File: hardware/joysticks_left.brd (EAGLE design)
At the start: 64.8 x 87.6 mm, 10 parts, among them IC1 MEGA16-M

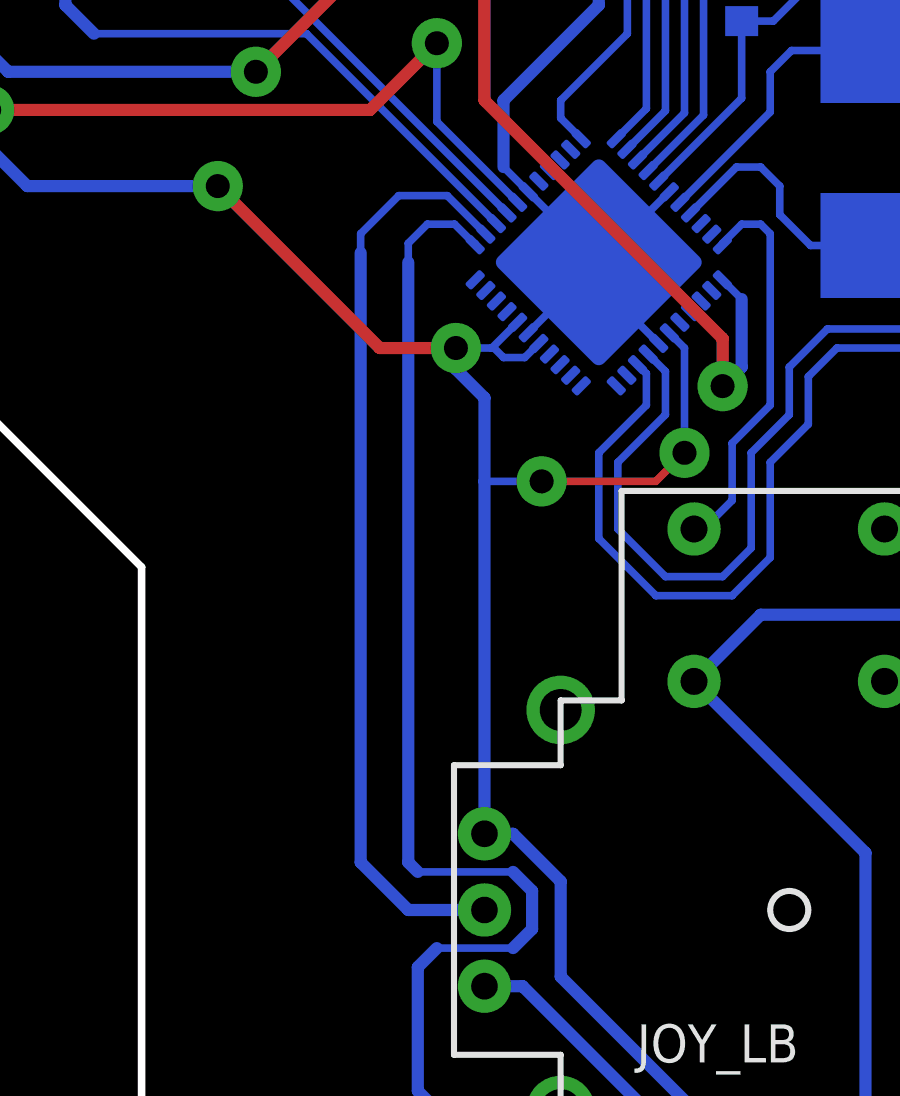
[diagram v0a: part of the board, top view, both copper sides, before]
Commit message: added mode selection jumper (SPI/I2C)
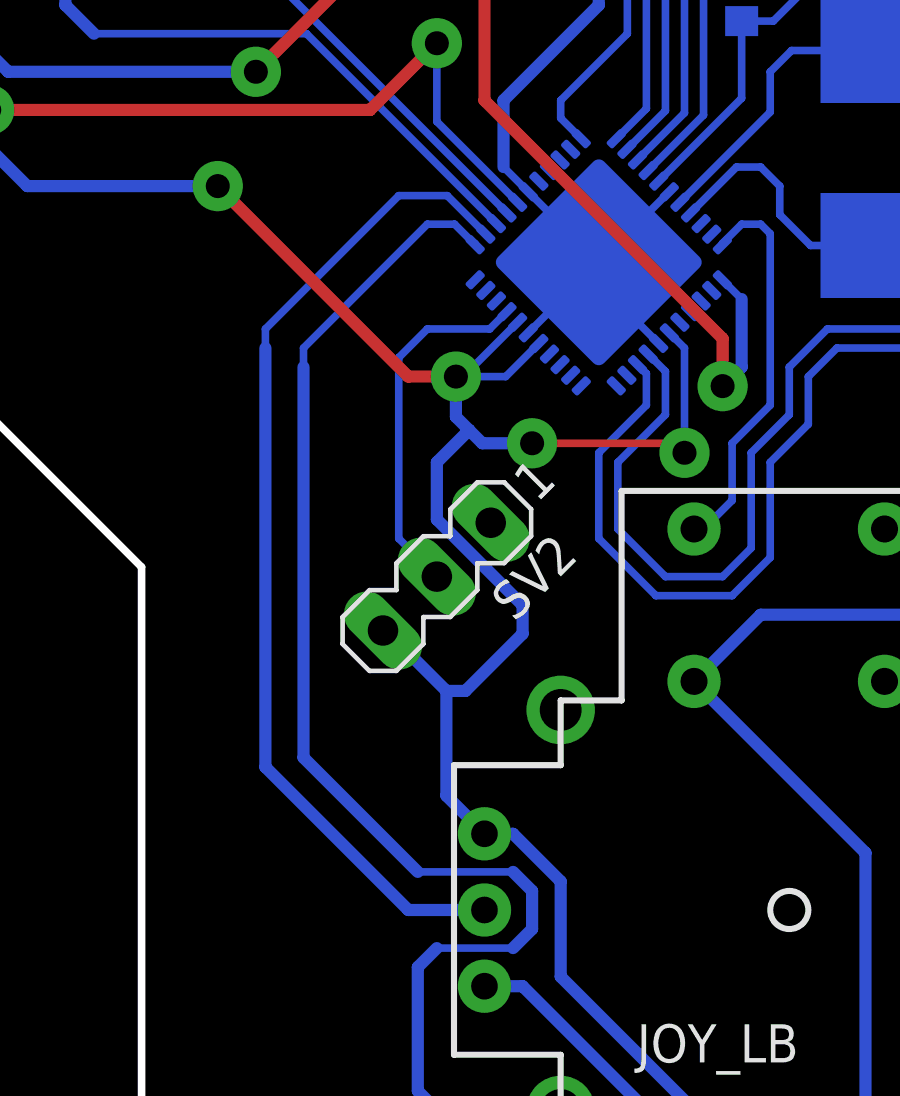
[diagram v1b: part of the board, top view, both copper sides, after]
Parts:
- added SV2: (no value), con-lstb:MA03-1
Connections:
- new net MD_SEL: IC1.30, SV2.2
- net GND: now also SV2.1
- net VCC: now also SV2.3
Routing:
- net MD_SEL: track 0.00 -> 12.1 mm
- net VCC: track 210.4 -> 218.4 mm
- net JOY_LB_H: track 54.8 -> 57.7 mm
- net JOY_LB_V: track 31.0 -> 33.6 mm
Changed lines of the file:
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@@
 <element name="U$2" library="holes" package="3,0" value="" x="30.1625" y="77.47"/>
 <element name="U$3" library="holes" package="3,0" value="" x="40.64" y="2.54"/>
+<element name="SV2" library="con-lstb" package="MA03-1" value="" x="28.8925" y="31.4325" rot="R225">
+<attribute name="OC_NEWARK" value="unknown" x="28.8925" y="31.4325" size="1.778" layer="27" rot="R225" display="off"/>
+<attribute name="MPN" value="" x="28.8925" y="31.4325" size="1.778" layer="27" rot="R225" display="off"/>
+<attribute name="MF" value="" x="28.8925" y="31.4325" size="1.778" layer="27" rot="R225" display="off"/>
+<attribute name="OC_FARNELL" value="unknown" x="28.8925" y="31.4325" size="1.778" layer="27" rot="R225" display="off"/>
+</element>
 </elements>
 <signals>
@@
 <vertex x="10.16" y="83.82"/>
 </polygon>
+<contactref element="SV2" pad="1"/>
 </signal>
 <signal name="VCC">
@@
 <wire x1="33.02" y1="18.0975" x2="38.1" y2="13.0175" width="0.4064" layer="16"/>
 <wire x1="38.1" y1="13.0175" x2="38.1" y2="10.16" width="0.4064" layer="16"/>
-<wire x1="30.48" y1="37.392890625" x2="30.48" y2="34.6075" width="0.4064" layer="16"/>
-<wire x1="30.48" y1="34.6075" x2="30.48" y2="22.86" width="0.4064" layer="16"/>
 <wire x1="31.58531875" y1="43.907575" x2="28.8925" y2="46.60039375" width="0.254" layer="16"/>
 <wire x1="28.8925" y1="46.60039375" x2="28.8925" y2="49.2125" width="0.254" layer="16"/>
@@
 <wire x1="22.86" y1="48.26" x2="14.605" y2="48.26" width="0.4064" layer="16"/>
 <wire x1="14.605" y1="48.26" x2="13.97" y2="48.895" width="0.4064" layer="16"/>
-<via x="29.5275" y="39.0525" extent="1-16" drill="0.8" diameter="1.6764"/>
-<wire x1="29.5275" y1="39.0525" x2="26.9875" y2="39.0525" width="0.4064" layer="1"/>
-<wire x1="26.9875" y1="39.0525" x2="21.59" y2="44.45" width="0.4064" layer="1"/>
+<via x="29.5275" y="38.1" extent="1-16" drill="0.8" diameter="1.6764"/>
+<wire x1="29.5275" y1="38.1" x2="27.94" y2="38.1" width="0.4064" layer="1"/>
+<wire x1="27.94" y1="38.1" x2="21.59" y2="44.45" width="0.4064" layer="1"/>
 <via x="21.59" y="44.45" extent="1-16" drill="0.8" diameter="1.6764"/>
 <wire x1="21.59" y1="44.45" x2="15.24" y2="44.45" width="0.4064" layer="16"/>
 <wire x1="15.24" y1="44.45" x2="13.97" y2="45.72" width="0.4064" layer="16"/>
 <wire x1="13.97" y1="45.72" x2="13.97" y2="46.99" width="0.4064" layer="16"/>
-<wire x1="30.48" y1="37.392890625" x2="29.5275" y2="38.345390625" width="0.4064" layer="16"/>
-<wire x1="29.5275" y1="38.345390625" x2="29.5275" y2="39.0525" width="0.4064" layer="16"/>
-<wire x1="31.58531875" y1="39.912421875" x2="30.725396875" y2="39.0525" width="0.254" layer="16"/>
-<wire x1="30.725396875" y1="39.0525" x2="29.5275" y2="39.0525" width="0.254" layer="16"/>
-<wire x1="32.292425" y1="39.205315625" x2="31.822109375" y2="38.735" width="0.254" layer="16"/>
-<wire x1="31.822109375" y1="38.735" x2="31.115" y2="38.735" width="0.254" layer="16"/>
-<wire x1="31.115" y1="38.735" x2="30.7975" y2="39.0525" width="0.254" layer="16"/>
-<wire x1="30.7975" y1="39.0525" x2="30.725396875" y2="39.0525" width="0.254" layer="16"/>
+<wire x1="29.5275" y1="36.757890625" x2="29.5275" y2="38.1" width="0.4064" layer="16"/>
 <wire x1="36.64113125" y1="39.55886875" x2="37.1475" y2="39.0525" width="0.254" layer="16"/>
 <wire x1="37.1475" y1="39.0525" x2="37.1475" y2="35.56" width="0.254" layer="16"/>
 <via x="37.1475" y="35.56" extent="1-16" drill="0.8" diameter="1.6764"/>
-<wire x1="37.1475" y1="35.56" x2="36.195" y2="34.6075" width="0.254" layer="1"/>
-<wire x1="36.195" y1="34.6075" x2="32.385" y2="34.6075" width="0.254" layer="1"/>
-<via x="32.385" y="34.6075" extent="1-16" drill="0.8" diameter="1.6764"/>
-<wire x1="32.385" y1="34.6075" x2="30.48" y2="34.6075" width="0.254" layer="16"/>
+<wire x1="37.1475" y1="35.56" x2="36.83" y2="35.8775" width="0.254" layer="1"/>
+<wire x1="36.83" y1="35.8775" x2="32.0675" y2="35.8775" width="0.254" layer="1"/>
+<via x="32.0675" y="35.8775" extent="1-16" drill="0.8" diameter="1.6764"/>
 <wire x1="51.1175" y1="45.72" x2="53.34" y2="45.72" width="0.254" layer="16"/>
+<contactref element="SV2" pad="3"/>
+<wire x1="31.58531875" y1="39.912421875" x2="29.772896875" y2="38.1" width="0.254" layer="16"/>
+<wire x1="29.772896875" y1="38.1" x2="29.5275" y2="38.1" width="0.254" layer="16"/>
+<wire x1="32.292425" y1="39.205315625" x2="31.187109375" y2="38.1" width="0.254" layer="16"/>
+<wire x1="31.187109375" y1="38.1" x2="29.5275" y2="38.1" width="0.254" layer="16"/>
+<wire x1="29.5275" y1="36.757890625" x2="29.967696875" y2="36.31769375" width="0.4064" layer="16"/>
+<wire x1="29.967696875" y1="36.31769375" x2="30.407890625" y2="35.8775" width="0.4064" layer="16"/>
+<wire x1="30.48" y1="22.86" x2="29.21" y2="24.13" width="0.4064" layer="16"/>
+<wire x1="29.21" y1="24.13" x2="29.21" y2="27.6225" width="0.4064" layer="16"/>
+<wire x1="27.196053125" y1="29.636446875" x2="27.096446875" y2="29.636446875" width="0.4064" layer="16"/>
+<wire x1="30.407890625" y1="35.8775" x2="32.0675" y2="35.8775" width="0.4064" layer="16"/>
+<wire x1="27.196053125" y1="29.636446875" x2="29.21" y2="27.6225" width="0.4064" layer="16"/>
+<wire x1="29.21" y1="27.6225" x2="29.845" y2="27.6225" width="0.4064" layer="16"/>
+<wire x1="29.845" y1="27.6225" x2="31.75" y2="29.5275" width="0.4064" layer="16"/>
+<wire x1="31.75" y1="29.5275" x2="31.75" y2="30.48" width="0.4064" layer="16"/>
+<wire x1="31.75" y1="30.48" x2="28.8925" y2="33.3375" width="0.4064" layer="16"/>
+<wire x1="28.8925" y1="33.3375" x2="28.8925" y2="35.2425" width="0.4064" layer="16"/>
+<wire x1="28.8925" y1="35.2425" x2="29.96769375" y2="36.31769375" width="0.4064" layer="16"/>
+<wire x1="29.96769375" y1="36.31769375" x2="29.967696875" y2="36.31769375" width="0.4064" layer="16"/>
 </signal>
 <signal name="BUT_LT">
@@
 <contactref element="IC1" pad="35"/>
 <wire x1="30.48" y1="20.32" x2="27.94" y2="20.32" width="0.4064" layer="16"/>
-<wire x1="27.94" y1="20.32" x2="26.3525" y2="21.9075" width="0.4064" layer="16"/>
-<wire x1="26.3525" y1="21.9075" x2="26.3525" y2="42.2275" width="0.4064" layer="16"/>
+<wire x1="27.94" y1="20.32" x2="23.1775" y2="25.0825" width="0.4064" layer="16"/>
+<wire x1="23.1775" y1="25.0825" x2="23.1775" y2="39.0525" width="0.4064" layer="16"/>
 <wire x1="30.524659375" y1="42.846915625" x2="29.239075" y2="44.1325" width="0.254" layer="16"/>
 <wire x1="29.239075" y1="44.1325" x2="27.6225" y2="44.1325" width="0.254" layer="16"/>
-<wire x1="27.6225" y1="44.1325" x2="26.3525" y2="42.8625" width="0.254" layer="16"/>
-<wire x1="26.3525" y1="42.8625" x2="26.3525" y2="42.2275" width="0.254" layer="16"/>
+<wire x1="27.6225" y1="44.1325" x2="23.1775" y2="39.6875" width="0.254" layer="16"/>
+<wire x1="23.1775" y1="39.6875" x2="23.1775" y2="39.0525" width="0.254" layer="16"/>
 </signal>
 <signal name="JOY_LB_H">
 <contactref element="JOY_LB" pad="H2"/>
 <contactref element="IC1" pad="34"/>
-<wire x1="27.94" y1="21.9075" x2="27.94" y2="41.91" width="0.4064" layer="16"/>
+<wire x1="24.4475" y1="25.4" x2="24.4475" y2="38.4175" width="0.4064" layer="16"/>
 <wire x1="30.171103125" y1="42.536396875" x2="30.171103125" y2="42.4933625" width="0.254" layer="16"/>
-<wire x1="27.94" y1="21.9075" x2="28.2575" y2="21.59" width="0.4064" layer="16"/>
+<wire x1="24.4475" y1="25.4" x2="28.2575" y2="21.59" width="0.4064" layer="16"/>
 <wire x1="28.2575" y1="21.59" x2="31.4325" y2="21.59" width="0.254" layer="16"/>
 <wire x1="31.4325" y1="21.59" x2="32.0675" y2="20.955" width="0.4064" layer="16"/>
@@
 <wire x1="30.171103125" y1="42.4933625" x2="29.484465625" y2="43.18" width="0.254" layer="16"/>
 <wire x1="29.484465625" y1="43.18" x2="28.575" y2="43.18" width="0.254" layer="16"/>
-<wire x1="28.575" y1="43.18" x2="27.94" y2="42.545" width="0.254" layer="16"/>
-<wire x1="27.94" y1="42.545" x2="27.94" y2="41.91" width="0.254" layer="16"/>
+<wire x1="28.575" y1="43.18" x2="24.4475" y2="39.0525" width="0.254" layer="16"/>
+<wire x1="24.4475" y1="39.0525" x2="24.4475" y2="38.4175" width="0.254" layer="16"/>
 </signal>
 <signal name="N$1">
@@
 <wire x1="39.155" y1="51.7525" x2="39.0525" y2="51.65" width="0.254" layer="16"/>
 </signal>
+<signal name="MD_SEL">
+<contactref element="IC1" pad="30"/>
+<contactref element="SV2" pad="2"/>
+<wire x1="31.231765625" y1="40.265975" x2="30.653290625" y2="39.6875" width="0.254" layer="16"/>
+<wire x1="30.653290625" y1="39.6875" x2="28.575" y2="39.6875" width="0.254" layer="16"/>
+<wire x1="28.575" y1="39.6875" x2="27.6225" y2="38.735" width="0.254" layer="16"/>
+<wire x1="27.6225" y1="38.735" x2="27.6225" y2="32.7025" width="0.254" layer="16"/>
+<wire x1="27.6225" y1="32.7025" x2="28.8925" y2="31.4325" width="0.254" layer="16"/>
+</signal>
 </signals>
